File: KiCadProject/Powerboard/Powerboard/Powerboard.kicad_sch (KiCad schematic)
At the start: 2 parts

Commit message: Refinement work, and start PCB layout
Signed-off-by: Eldalote.Electronics <Eldalote.Electronics@gmail.com>
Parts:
- added C1: 10u, Capacitor_SMD:C_1206_3216Metric, symbol Device:C_Small
- added C2: 2u2, Capacitor_SMD:C_0603_1608Metric, symbol Device:C_Small
- added C3: 220n/390n, Capacitor_SMD:C_0805_2012Metric, symbol Device:C_Small
- added C4, C5, C6, C7: 4u7, Capacitor_SMD:C_1206_3216Metric, symbol Device:C_Small
- added D1: D_Schottky, Diode_SMD:D_PowerDI-5, symbol Device:D_Schottky
- added J3: Conn_01x03_Male, Connector_PinHeader_2.54mm:PinHeader_1x03_P2.54mm_Vertical, symbol Connector:Conn_01x03_Male
- added L1: SRP1265C-6R8M, Eldalote-footprints:SRP-1265C, symbol pspice:INDUCTOR
- added Q1: SIR696DP-T1-GE3, Ultralibrarianfootprints:SIR696DP-T1-GE3, symbol 2022-11-21_10-21-02:SIR696DP-T1-GE3
- added Q2: SUD50P10-43L-GE3, Package_TO_SOT_SMD:TO-252-2, symbol Device:Q_PMOS_GDS
- added R1, R3, R9: 100k, Resistor_SMD:R_0603_1608Metric, symbol Device:R
- added R10: 330m/130m, Resistor_SMD:R_1206_3216Metric, symbol Device:R
- added R2: 7k3, Resistor_SMD:R_0603_1608Metric, symbol Device:R
- added R4: 953R/120R, Resistor_SMD:R_0402_1005Metric, symbol Device:R
- added R5: 4k7/2k7, Resistor_SMD:R_0603_1608Metric, symbol Device:R
- added R6: 51m/33m, Resistor_SMD:R_0603_1608Metric, symbol Device:R
- added R7: 100R, Resistor_SMD:R_0805_2012Metric, symbol Device:R
- added R8: 5M1/4M75, Resistor_SMD:R_0603_1608Metric, symbol Device:R
- added U1: MAX16833, Package_SO:HTSSOP-16-1EP_4.4x5mm_P0.65mm_EP3.4x5mm_Mask2.46x2.31mm_ThermalVias, symbol Eldalote_symbols:MAX16833A
- gave numbers to parts that had none: 2
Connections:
- net GND: now reaches J1.N
- net GND: now also J2.1 (N), C1.2, C2.1, C4.2, C5.2, C6.2, C7.2, J3.1 (Pin_1), R1.1, R2.1, R4.1, R6.1, R9.1, U1.1 (LFRAMP), U1.13 (PGND), U1.17 (EP), U1.3 (SGND)
- net IN: now reaches J1.P
- net IN: now also C1.1, L1.1, U1.16 (IN)
- net LED+: now reaches J2.2 (P)
- net LED+: now also Q2.2 (D)
- new net: D1.2 (A), L1.2, Q1.5, Q1.6, Q1.7, Q1.8
- new net !DIMOUT: Q2.1 (G), U1.9 (!DIMOUT)
- new net !FTL: J3.3 (Pin_3), U1.6 (!FTL)
- new net COMP: C3.1, U1.5 (COMP)
- new net CS: R5.1, U1.12 (CS)
- new net ICTRL: R1.2, R3.1, U1.4 (ICTRL)
- new net ISENSE+: C4.1, C5.1, C6.1, C7.1, D1.1 (K), R10.2, R8.2, U1.11 (ISENSE+)
- new net ISENSE-: R7.1, U1.10 (ISENSE-)
- new net ISENSE-R: Q2.3 (S), R10.1, R7.2
- new net NDRV: Q1.4, U1.14 (NDRV)
- new net OPV: R8.1, R9.2, U1.8 (OVP)
- new net PWMDIM: J3.2 (Pin_2), U1.7 (PWMDIM)
- new net RCS: Q1.1, Q1.2, Q1.3, R5.2, R6.2
- new net RT/SYNC: R2.2, U1.2 (RT/SYNC)
- new net VCC: C2.2, R3.2, U1.15 (VCC)
- new net comp_RC: C3.2, R4.2
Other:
- removed sheet LED Driver
- note added: "AV*"
- note added: "AV*: Alternative values: First value is for the LED board (~64v 0.9A), second value is for the monolithic LED (~51V, 1.7A)"
- note added: "Component value calculations aided by application note 5571 and the provided excel sheet"
- note added: "Connector with control signals"
- note added: "Note: R8=R9, precise value not important"
- note added: "Output Caps"
- note added: "XT30 connector to LED(s)"
- note removed: "To LED(s)"
- moved on the sheet: J1, J2

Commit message: Much more refinement. Re-selected some components for more logical ones. Got all 3d models in place.
Signed-off-by: Eldalote.Electronics <Eldalote.Electronics@gmail.com>
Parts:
- removed Q1: SIR696DP-T1-GE3, Ultralibrarianfootprints:SIR696DP-T1-GE3, symbol 2022-11-21_10-21-02:SIR696DP-T1-GE3
- added C1: Connector cap, Capacitor_SMD:CP_Elec_5x5.3, symbol Device:C_Small
- added C3: 100n, Capacitor_SMD:C_0402_1005Metric, symbol Device:C_Small
- added NT1: NetTie_2, NetTie:NetTie-2_SMD_Pad0.5mm, symbol Device:NetTie_2
- added Q1: Q_NMOS_GDS, Package_TO_SOT_SMD:TO-252-2, symbol Device:Q_NMOS_GDS
- C2: renamed from C1; mfid UMK325AB7106MMHP -> (none)
- C4: renamed from C2; footprint Capacitor_SMD:C_0603_1608Metric -> Capacitor_SMD:C_0402_1005Metric
- C5: renamed from C3; value 220n/390n -> 220n; footprint Capacitor_SMD:C_0805_2012Metric -> Capacitor_SMD:C_0603_1608Metric; AltValue (none) -> 390n
- L1: value SRP1265C-6R8M -> 6u8
- R1: renamed from R3; footprint Resistor_SMD:R_0603_1608Metric -> Resistor_SMD:R_0402_1005Metric
- R10: value 330m/130m -> 330m; AltValue (none) -> 130m
- R2: renamed from R1; footprint Resistor_SMD:R_0603_1608Metric -> Resistor_SMD:R_0402_1005Metric
- R3: renamed from R2; footprint Resistor_SMD:R_0603_1608Metric -> Resistor_SMD:R_0402_1005Metric
- R4: value 953R/120R -> 953R; AltValue (none) -> 120R
- R5: value 4k7/2k7 -> 4k7; footprint Resistor_SMD:R_0603_1608Metric -> Resistor_SMD:R_0402_1005Metric; AltValue (none) -> 2k7
- R6: value 51m/33m -> 51m; footprint Resistor_SMD:R_0603_1608Metric -> Resistor_SMD:R_1206_3216Metric; AltValue (none) -> 33m
- R7: footprint Resistor_SMD:R_0805_2012Metric -> Resistor_SMD:R_0603_1608Metric
- R8: value 5M1/4M75 -> 5M1; AltValue (none) -> 4M75
- R9: footprint Resistor_SMD:R_0603_1608Metric -> Resistor_SMD:R_0402_1005Metric
- U1: symbol Eldalote_symbols:MAX16833A -> Eldalote_symbols:MAX16833
- renumbered C4 to C6, C5 to C7, C6 to C8, C7 to C9
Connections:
- net GND: now also C1.2, C3.2
- net IN: now also C1.1, C3.1
- net ISENSE+: now also NT1.1; no longer C6.1, C7.1, C8.1, C9.1, D1.1 (K), R10.2, R8.2
- net NDRV: now also Q1.1 (G)
- net RCS: now also Q1.3 (S)
- net L-out: now reaches D1.2 (A), L1.2
- net L-out: now also Q1.2 (D)
- net ISENSE-R renamed Vout-FET
- new net V-out: C6.1, C7.1, C8.1, C9.1, D1.1 (K), NT1.2, R10.2, R8.2
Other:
- note added: "100kHz Selection Resistor: 7350KOhm/R(7.35KOhm) = Fosc in kHz"
- note added: "Alternative Values: Several components have alternative values listed (in purple). The main value is the value calculated for the 10-LED PCB (~65V 0.9A) The Alt value is the value calculated for the monolithic LED (~51V 1.7A)"
- note added: "Battery(manager) power Input"
- note added: "Compensation RC"
- note added: "Component layout in similar positions as in the MAX16833 datasheet"
- note added: "LED current sense"
- note added: "Note: Resistors the same, exact value not important"
- note added: "Overvoltage protection"
- note added: "Switch current sense"
- note removed: "AV*"
- note removed: "AV*: Alternative values: First value is for the LED board (~64v 0.9A), second value is for the monolithic LED (~51V, 1.7A)"
- note removed: "Battery power Input"
- note removed: "Note: R8=R9, precise value not important"
- moved on the sheet: C2, C4, C5, C6, C7, C8, C9, D1, J1, J2, J3, L1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

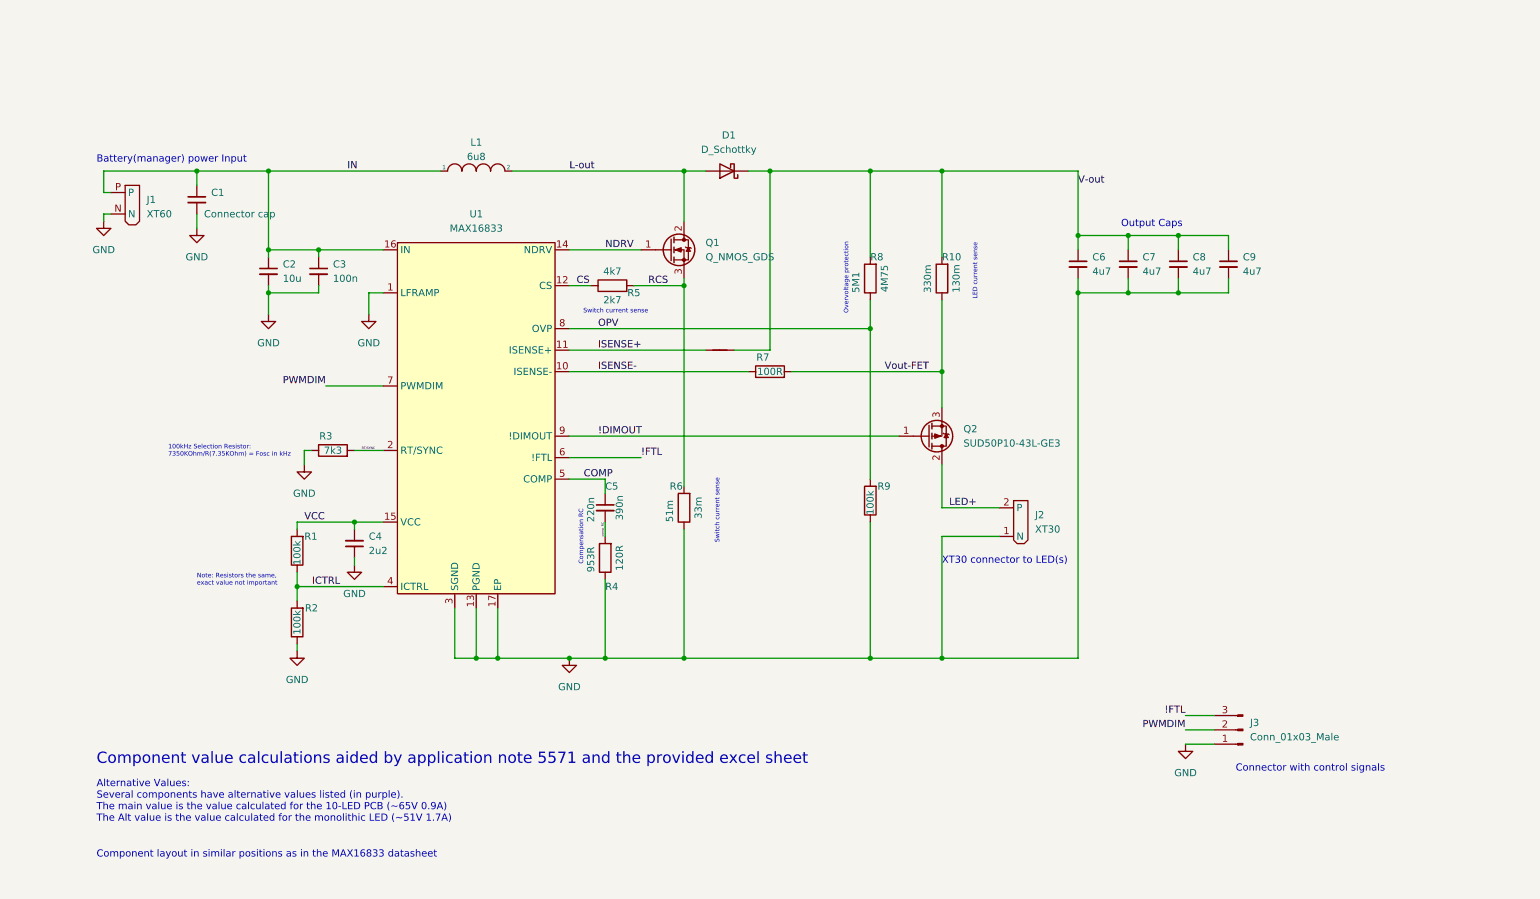
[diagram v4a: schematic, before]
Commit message: Should be final placement on powerboard now, just finishing touches left.
Signed-off-by: Eldalote.Electronics <Eldalote.Electronics@gmail.com>
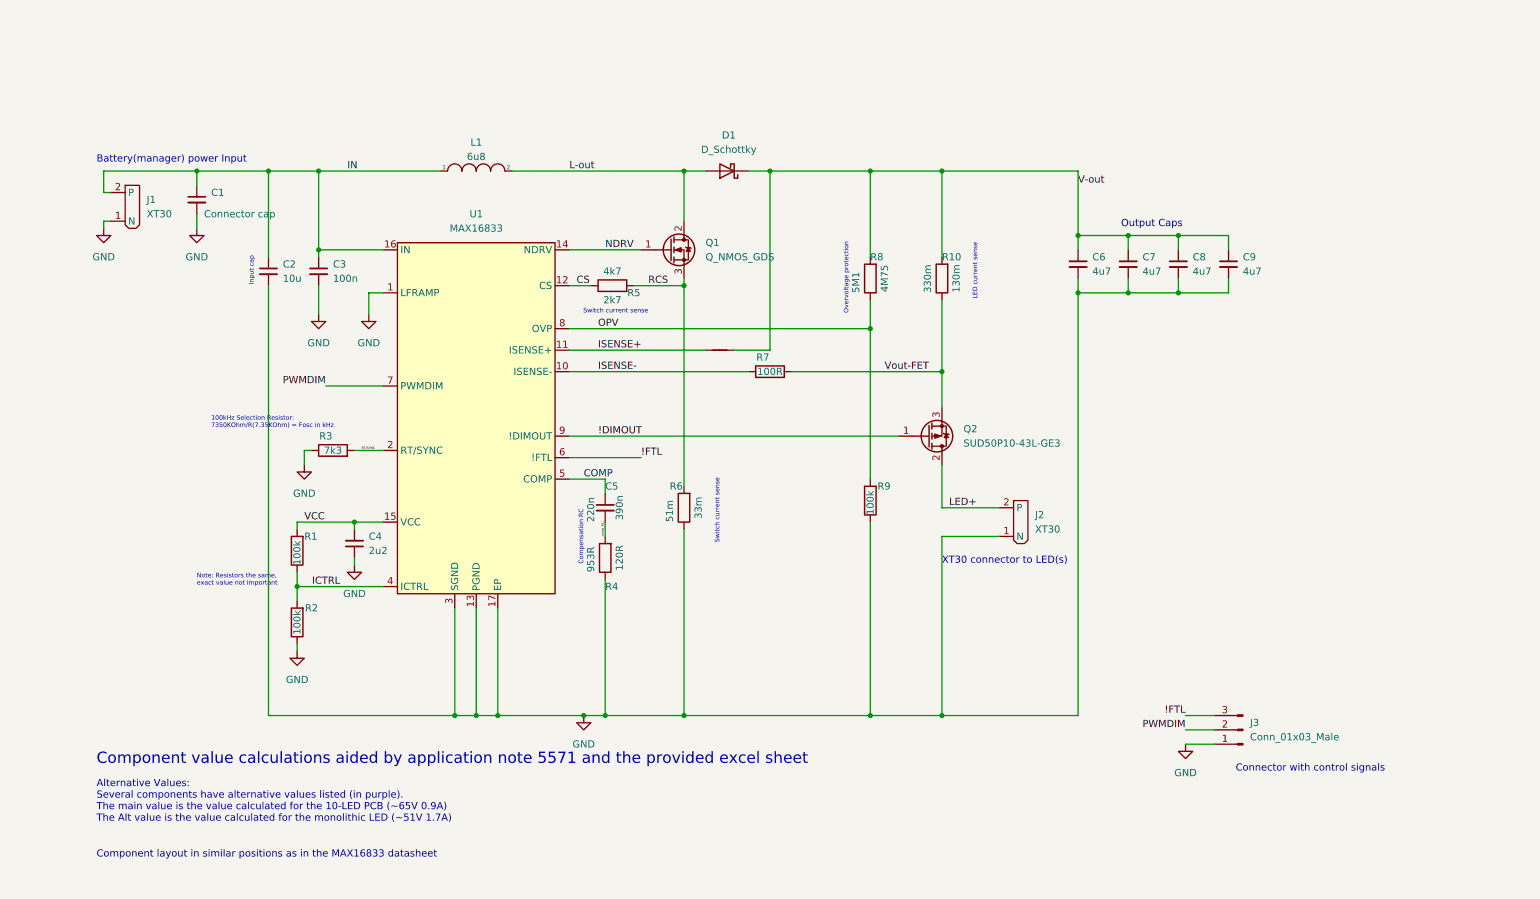
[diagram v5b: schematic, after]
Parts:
- removed J1: XT60, Eldalote-footprints:XT60, symbol Eldalote_symbols:XT60
- added J1: XT30, Eldalote-footprints:XT30, symbol Eldalote_symbols:XT30
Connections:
- net GND: now also J1.1 (N)
- net IN: now also J1.2 (P)
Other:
- note added: "Input cap"

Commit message: Led driver board v0.1 done
Signed-off-by: Eldalote.Electronics <Eldalote.Electronics@gmail.com>
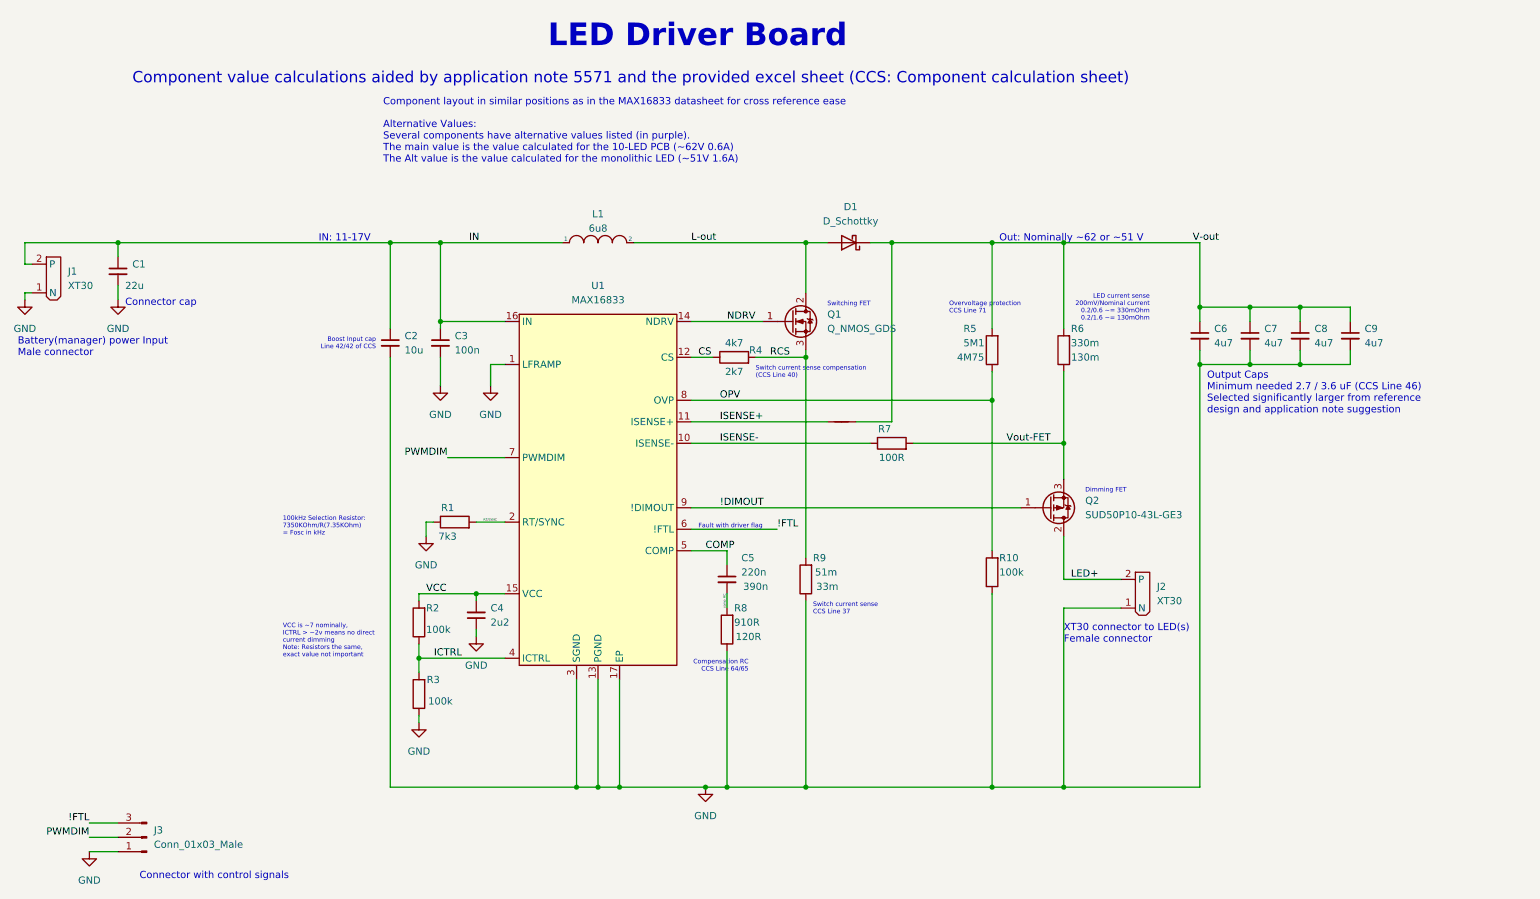
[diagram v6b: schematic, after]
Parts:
- C1: value Connector cap -> 22u
- J2: footprint Eldalote-footprints:XT30 -> Eldalote-footprints:XT30_Female
- R8: renamed from R4; value 953R -> 910R
- renumbered R3 to R1, R9 to R10, R1 to R2, R2 to R3, R5 to R4, R8 to R5, R10 to R6, R6 to R9
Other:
- note added: "Alternative Values: Several components have alternative values listed (in purple). The main value is the value calculated for the 10-LED PCB (~62V 0.6A) The Alt value is the value calculated for the monolithic LED (~51V 1.6A)"
- note added: "Battery(manager) power Input Male connector"
- note added: "Boost Input cap Line 42/42 of CCS"
- note added: "Compensation RC CCS Line 64/65"
- note added: "Component layout in similar positions as in the MAX16833 datasheet for cross reference ease"
- note added: "Component value calculations aided by application note 5571 and the provided excel sheet (CCS: Component calculation sheet)"
- note added: "Connector cap"
- note added: "Dimming FET"
- note added: "Fault with driver flag"
- note added: "IN: 11-17V"
- note added: "LED Driver Board"
- note added: "LED current sense 200mV/Nominal current 0.2/0.6 ~= 330mOhm 0.2/1.6 ~= 130mOhm"
- note added: "Out: Nominally ~62 or ~51 V"
- note added: "Output Caps Minimum needed 2.7 / 3.6 uF (CCS Line 46) Selected significantly larger from reference design and application note suggestion"
- note added: "Overvoltage protection CCS Line 71"
- note added: "Switch current sense CCS Line 37"
- note added: "Switch current sense compensation (CCS Line 40)"
- note added: "Switching FET"
- note added: "VCC is ~7 nominally, ICTRL > ~2v means no direct current dimming Note: Resistors the same, exact value not important"
- note added: "XT30 connector to LED(s) Female connector"
- note removed: "Alternative Values: Several components have alternative values listed (in purple). The main value is the value calculated for the 10-LED PCB (~65V 0.9A) The Alt value is the value calculated for the monolithic LED (~51V 1.7A)"
- note removed: "Battery(manager) power Input"
- note removed: "Compensation RC"
- note removed: "Component layout in similar positions as in the MAX16833 datasheet"
- note removed: "Component value calculations aided by application note 5571 and the provided excel sheet"
- note removed: "Input cap"
- note removed: "LED current sense"
- note removed: "Note: Resistors the same, exact value not important"
- note removed: "Output Caps"
- note removed: "Overvoltage protection"
- note removed: "Switch current sense"
- note removed: "XT30 connector to LED(s)"
- title: (none) -> LED Driver Board
- moved on the sheet: C2, C3, C4, C5, C6, C7, C8, C9, D1, J2, J3, L1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
